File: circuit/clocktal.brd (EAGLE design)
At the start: 100 x 80 mm, 28 parts, among them IC1 PIC16F688, Q1 8.0

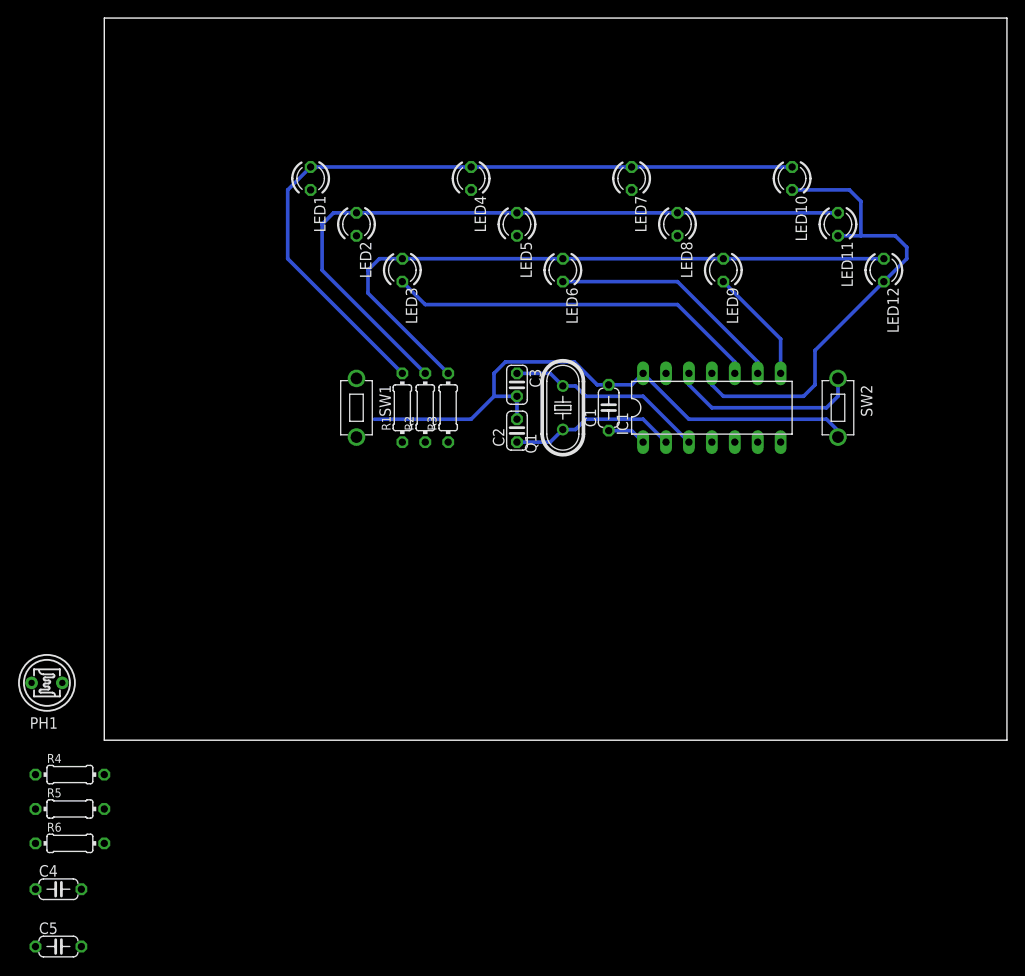
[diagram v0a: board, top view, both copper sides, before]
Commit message: added Single Sided PCB design
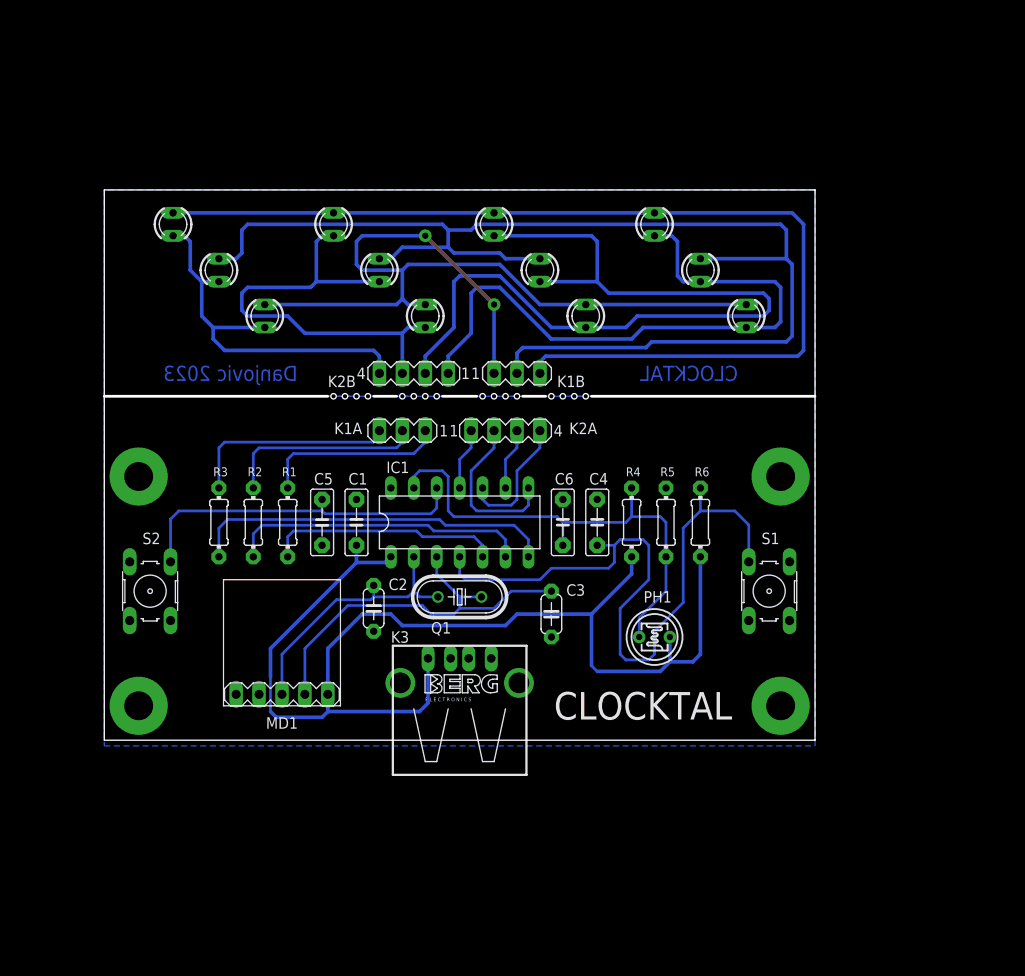
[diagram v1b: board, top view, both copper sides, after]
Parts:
- removed SW1, SW2: (no value), tactile:2PST_MINI
- added C6: 100n, rcl:C050-025X75L
- added K1A, K1B: (no value), con-lstb:MA03-1
- added K2A, K2B: (no value), con-lstb:MA04-1
- added K3: PN87520-S, con-berg:PN87520-S
- added MD1: (no value), RTC:RTC-DS3231-SMALL_L
- added S1, S2: (no value), switch-omron:B3F-10XX
- C1, C4, C5: device rcl:C050-024X044 -> rcl:C050-025X75L
- C2, C3: device rcl:C025-024X044 -> rcl:C050-024X044L
- LED1, LED10, LED11, LED12, LED2, LED3, LED4, LED5, LED6, LED7, LED8, LED9: device led:LED3MM -> led:LED3MM_L
- R1, R2, R3, R4, R5: device rcl:0204/7 -> rcl:0204/7L
- R6: value 10k -> 15k; device rcl:0204/7 -> rcl:0204/7L
- moved R6 78.4 mm to (66.0, 24.1), turned to 90 degrees
- moved R5 73.3 mm to (62.2, 24.1), turned to 270 degrees
- moved C4 72.2 mm to (54.6, 24.1), turned to 90 degrees
- moved R4 68.2 mm to (58.4, 24.1), turned to 90 degrees
- moved PH1 67.5 mm to (61.0, 11.4), turned to 180 degrees
- moved C5 55.3 mm to (24.1, 24.1), turned to 270 degrees
- moved IC1 30.7 mm to (39.4, 24.1)
- moved C1 30.7 mm to (27.9, 24.1)
- moved R3 28.4 mm to (12.7, 24.1)
- moved C3 25.7 mm to (49.5, 14.0)
- moved C2 25.3 mm to (29.8, 14.6), turned to 270 degrees
- moved Q1 23.9 mm to (39.4, 15.9), turned to 0 degrees
- moved R2 22.9 mm to (16.5, 24.1)
- moved R1 18.0 mm to (20.3, 24.1)
- moved LED1 16.1 mm to (7.62, 57.1)
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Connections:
- removed net XT1: C2.1, IC1.2, Q1.1
- removed net XT2: C3.1, IC1.3, Q1.2
- new net BIT0A: K1A.1, R1.2
- new net BIT1A: K1A.2, R2.2
- new net BIT2A: K1A.3, R3.2
- new net DGT0: K2B.1, LED10.K, LED11.K, LED12.K
- new net DGT1: K2B.2, LED7.K, LED8.K, LED9.K
- new net DGT2: K2B.3, LED4.K, LED5.K, LED6.K
- new net DGT3: K2B.4, LED1.K, LED2.K, LED3.K
- new net XT1/SCL: C2.1, IC1.2, MD1.J1.3, Q1.1
- new net XT2/SDA: C3.1, IC1.3, MD1.J1.2, Q1.2
- net +5V: now also K3.1, MD1.J1.1
- net B0: now also K1B.1; no longer R3.2
- net B1: now also K1B.2; no longer R2.2
- net B2: now also K1B.3; no longer R1.2
- net BIT0: now also R1.1; no longer R3.1
- net BIT2: now also R3.1; no longer R1.1
- net BUTTON1: now also S1.2; no longer SW1.P$2
- net BUTTON2: now also S2.4; no longer SW2.P$2
- net DIGIT0: now also K2A.1; no longer LED10.K, LED11.K, LED12.K
- net DIGIT1: now also K2A.2; no longer LED7.K, LED8.K, LED9.K
- net DIGIT2: now also K2A.3; no longer LED4.K, LED5.K, LED6.K
- net DIGIT3: now also K2A.4; no longer LED1.K, LED2.K, LED3.K
- net GND: now also C6.2, K3.4, K3.S1, K3.S2, MD1.J1.5, S1.4, S2.2; no longer SW1.P$1, SW2.P$1
- net LDR: now also C6.1
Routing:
- net +5V: track 4.34 -> 129.1 mm
- net DGT1: track 0.00 -> 93.4 mm
- net BUTTON1: track 0.00 -> 76.6 mm
- net DGT0: track 0.00 -> 70.0 mm
- net GND: track 64.8 -> 0.00 mm
- net B1: track 78.9 -> 142.5 mm
- net LDR: track 0.00 -> 54.2 mm
- net DGT2: track 0.00 -> 50.4 mm
- net DIGIT0: track 53.3 -> 6.88 mm
- net XT2/SDA: track 0.00 -> 45.0 mm
- net DGT3: track 0.00 -> 42.7 mm
- net BIT2: track 0.00 -> 40.7 mm
- net BIT1: track 0.00 -> 33.4 mm
- net B2: track 82.5 -> 115.4 mm
- net XT1/SCL: track 0.00 -> 30.0 mm
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- added copper zone on layer 16, net GND
- added copper zone on layer 16, net N$4
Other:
- board size 100 x 80 mm -> 78.7 x 61 mm
- board text added: "CLOCKTAL"
- board text added: "Danjovic 2023"

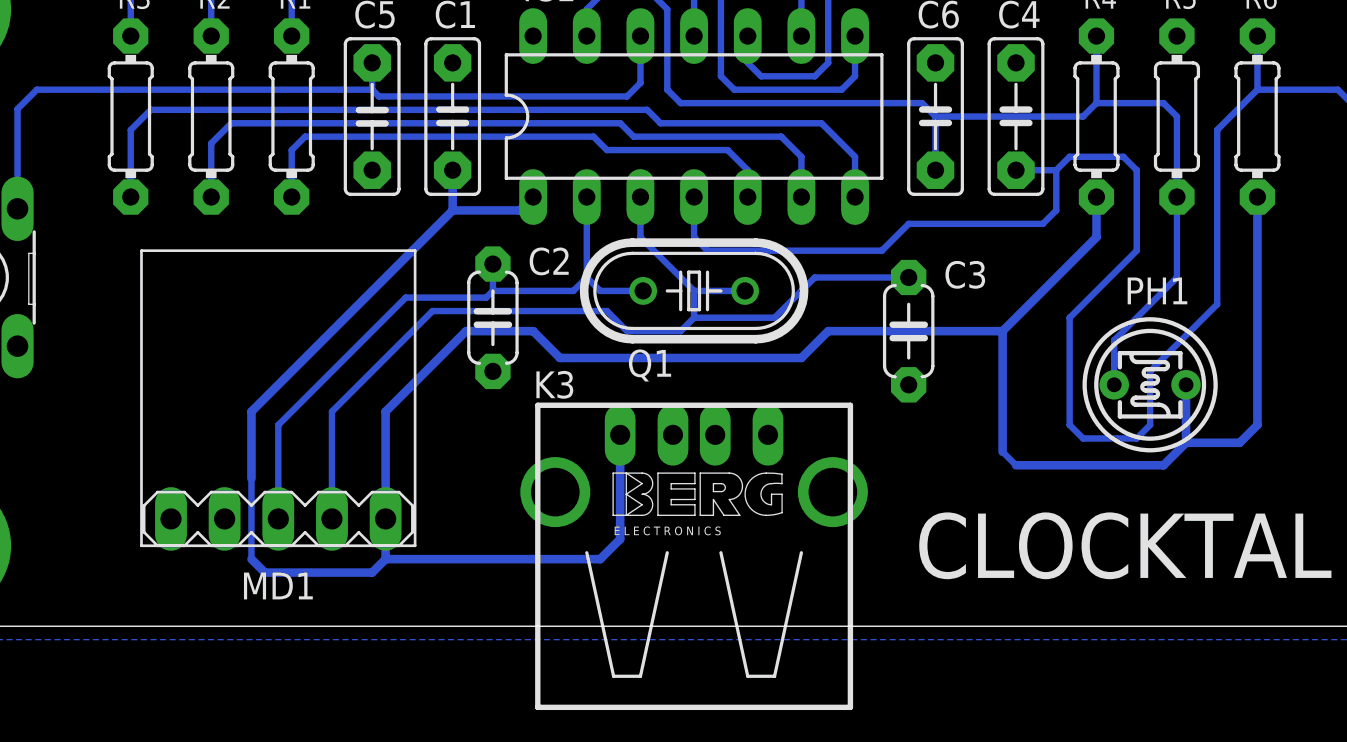
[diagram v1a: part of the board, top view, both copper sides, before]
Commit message: Improved PCB aesthetics
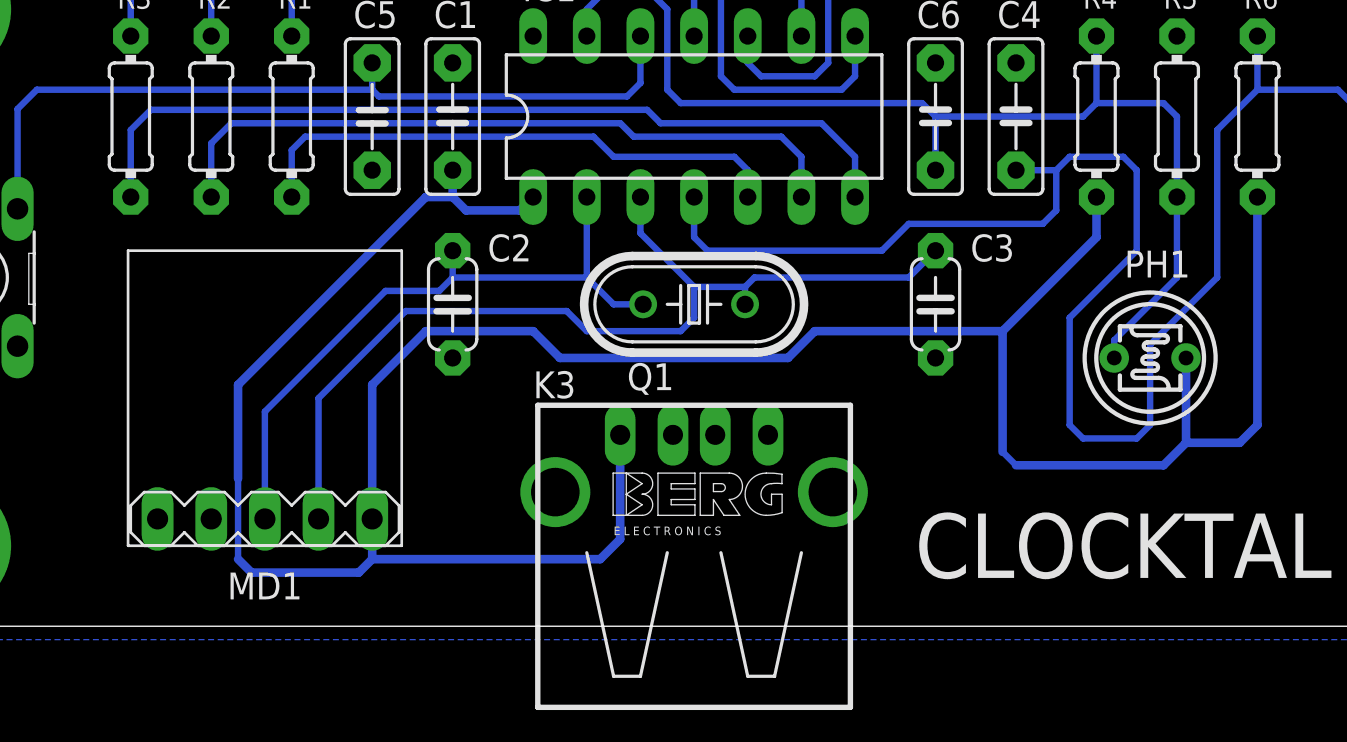
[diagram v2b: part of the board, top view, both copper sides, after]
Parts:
- moved C2 2.01 mm to (27.9, 15.2)
- moved C3 1.80 mm to (50.8, 15.2)
- moved PH1 1.27 mm to (61.0, 12.7)
- moved Q1 0.63 mm to (39.4, 15.2)
- moved MD1 0.63 mm to (19.1, 11.4)
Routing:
- net +5V: track 129.1 -> 133.7 mm
- net LDR: track 54.2 -> 53.0 mm
- net XT1/SCL: track 30.0 -> 31.2 mm
- net XT2/SDA: track 45.0 -> 45.6 mm
